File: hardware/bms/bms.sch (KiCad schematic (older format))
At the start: 91 parts

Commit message: Schematics update
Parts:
- added C? (x3): 4.7nF, Capacitor_SMD:C_0603_1608Metric_Pad1.05x0.95mm_HandSolder, symbol Device:C
- added C?: 330uF, Capacitor_Tantalum_SMD:CP_EIA-3528-21_Kemet-B, symbol Device:CP1
- added C?: 1nF, Capacitor_SMD:C_0603_1608Metric_Pad1.05x0.95mm_HandSolder, symbol Device:C
- added C?: 2.2uF, Capacitor_SMD:C_0603_1608Metric_Pad1.05x0.95mm_HandSolder, symbol Device:C
- added D? (x3): MBR340, Diode_THT:D_DO-201AD_P15.24mm_Horizontal, symbol Diode:MBR340
- added JP? (x5): JUMPER, symbol BMS:JUMPER
- added L?: 100uH, symbol pspice:INDUCTOR
- added Q? (x3): Q_NMOS_DGS, symbol Device:Q_NMOS_DGS
- added Q?: Q_PMOS_GSD, symbol BMS:Q_PMOS_GSD
- added Q?: BC817, Package_TO_SOT_SMD:SOT-23, symbol Transistor_BJT:BC817
- added Q?: BS170, Package_TO_SOT_THT:TO-92_Inline, symbol Transistor_FET:BS170
- added R? (x5): 10K, Resistor_SMD:R_0603_1608Metric_Pad1.05x0.95mm_HandSolder, symbol Device:R_Small
- added R? (x6): 1K, Resistor_SMD:R_0603_1608Metric_Pad1.05x0.95mm_HandSolder, symbol Device:R_Small
- added R? (x3): 1M, Resistor_SMD:R_0603_1608Metric_Pad1.05x0.95mm_HandSolder, symbol Device:R_Small
- added R?: 100E, Resistor_SMD:R_0603_1608Metric_Pad1.05x0.95mm_HandSolder, symbol Device:R_Small
- added R? (x2): 499, Resistor_SMD:R_0603_1608Metric_Pad1.05x0.95mm_HandSolder, symbol Device:R_Small
- added R?: 0.002E, Resistor_SMD:R_0603_1608Metric_Pad1.05x0.95mm_HandSolder, symbol Device:R_Small
- added TP? (x2): TestPoint, symbol Connector:TestPoint
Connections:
- net labels added: C1, C1-, C2, C3, C4, C5, C6, C7, C8, CFET, CHG, CHMON, CS1, CS2, DFET, EOC, FETSOFF, INT, LDMON, LOAD, PCFET, PSD, PWM, PWR+, SD, VDD
- net labels removed: CELL1, CELL1-, CELL2, CELL3, CELL4, CELL5, CELL6, CELL7, CELL8, PWM1
- wire segments 329 -> 502
- no-connect marks 4 -> 6
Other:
- note added: "<= 4 Cells"
- note added: "<= 5 Cells"
- note added: "<= 6 Cells"
- note added: "<= 7 Cells"
- note added: "== 3 Cells"
- moved on the sheet: C?

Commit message: added packin and packout
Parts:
- removed J?: Conn_01x10, symbol Connector_Generic:Conn_01x10
- added J? (x4): Conn_01x02, symbol BMS:Conn_01x02
- added J?: Conn_01x10, symbol Connector_Generic:Conn_01x10
- added J?: Conn_01x06, symbol BMS:Conn_01x06
- added J?: Conn_01x04, symbol Connector_Generic:Conn_01x04
- added J?: PACK_OUT, symbol Connector_Generic:Conn_01x04
- added J?: PACK_IN, symbol Connector_Generic:Conn_01x04
- added JP?: JUMPER3, symbol BMS:JUMPER3
- added R?: 2K2, Resistor_SMD:R_0603_1608Metric_Pad1.05x0.95mm_HandSolder, symbol Device:R_Small
- added R?: 300K, Resistor_SMD:R_0603_1608Metric_Pad1.05x0.95mm_HandSolder, symbol Device:R_Small
- added R?: 20K, Resistor_SMD:R_0603_1608Metric_Pad1.05x0.95mm_HandSolder, symbol Device:R_Small
- JP? (x6): symbol BMS:JUMPER -> bms-rescue:JUMPER-BMS
- Q? (x4): symbol BMS:Q_PMOS_GSD -> bms-rescue:Q_PMOS_GSD-BMS
- U?: symbol BMS:LSI94202 -> bms-rescue:LSI94202-BMS
- U?: symbol BMS:TPS560430 -> bms-rescue:TPS560430-BMS
- U?: symbol BMS:USBLC6-2SC6 -> bms-rescue:USBLC6-2SC6-BMS
- Y?: symbol BMS:Crystal -> bms-rescue:Crystal-BMS
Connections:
- net labels added: 485_TX_EN, ADC_PWR, PACK_ID
- net labels removed: ADC, GPIO1, GPIO10, GPIO11, GPIO2, GPIO3, GPIO4, GPIO5
- wire segments 502 -> 558
- no-connect marks 6 -> 8
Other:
- note added: "PACK ID ADC"

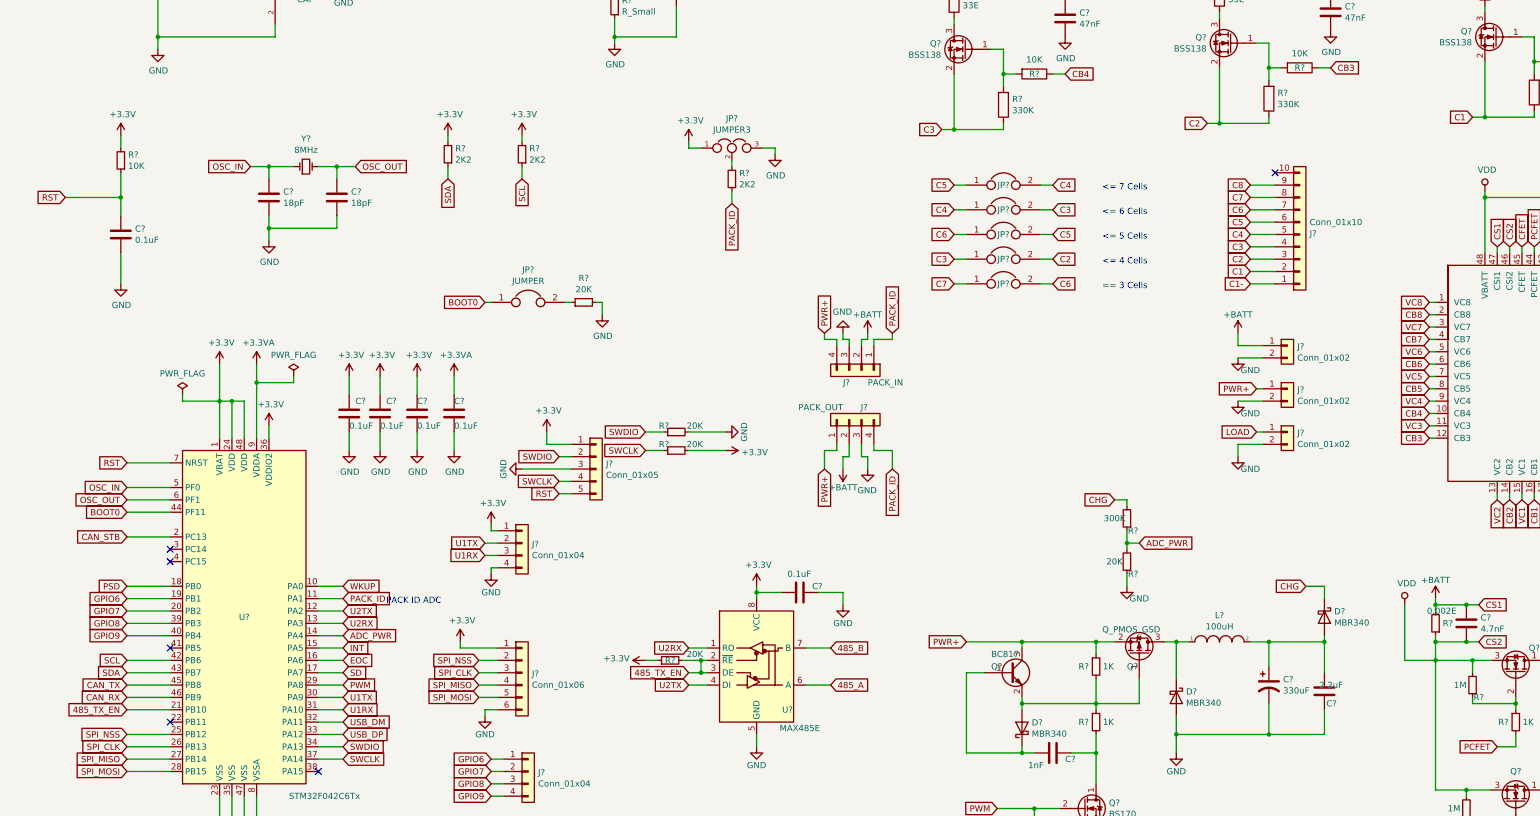
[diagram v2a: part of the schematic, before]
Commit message: Updated power control
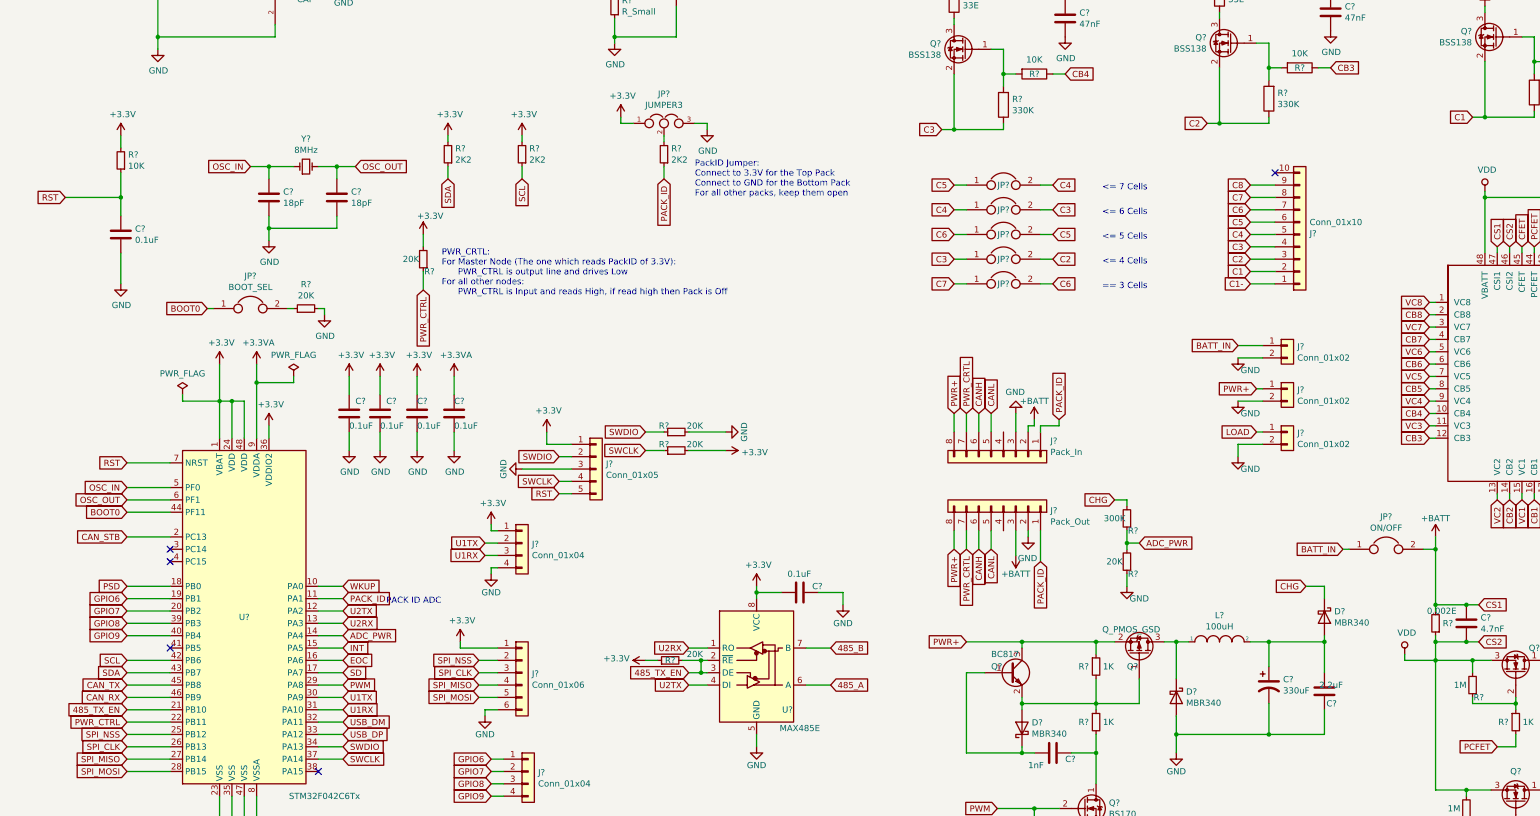
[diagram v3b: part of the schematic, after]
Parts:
- removed J?: PACK_OUT, symbol Connector_Generic:Conn_01x04
- removed J?: PACK_IN, symbol Connector_Generic:Conn_01x04
- added J?: Pack_In, symbol Connector_Generic:Conn_01x08
- added J?: Pack_Out, symbol Connector_Generic:Conn_01x08
- added JP?: ON/OFF, symbol BMS:JUMPER
- added R?: 20K, Resistor_SMD:R_0603_1608Metric_Pad1.05x0.95mm_HandSolder, symbol Device:R_Small
- JP?: value JUMPER -> BOOT_SEL
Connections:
- net +3V3: now also R?.2
- net +BATT: now also J?.2 (Pin_2), J?.3 (Pin_3), JP?.2; no longer J?.1 (Pin_1)
- net CANH: now also J?.6 (Pin_6), J?.6 (Pin_6)
- net CANL: now also J?.5 (Pin_5), J?.5 (Pin_5)
- net GND: now also J?.2 (Pin_2), J?.3 (Pin_3)
- net PACK_ID: now also J?.1 (Pin_1), J?.1 (Pin_1)
- net PWR+: now also J?.8 (Pin_8), J?.8 (Pin_8)
- net PWR_CTRL: now reaches U?.22 (PB11)
- net PWR_CTRL: now also R?.1
- new net BATT_IN: J?.1 (Pin_1), JP?.1
- new net PWR_CRTL: J?.7 (Pin_7), J?.7 (Pin_7)
- no-connect marks 8 -> 7
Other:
- note added: "PWR_CRTL:\nFor Master Node (The one which reads PackID of 3.3V):\n PWR_CTRL is output line and drives Low\nFor all other nodes:\n PWR_CTRL is Input and reads High, if read high then Pack is Off"
- note added: "PackID Jumper:\nConnect to 3.3V for the Top Pack\nConnect to GND for the Bottom Pack\nFor all other packs, keep them open"
- moved on the sheet: JP?, R?

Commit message: added indication leds
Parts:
- removed J?: Conn_01x04, symbol Connector_Generic:Conn_01x04
- added D? (x5): LED, LED_SMD:LED_0805_2012Metric, symbol Device:LED
- added JP? (x2): JUMPER3, symbol BMS:JUMPER3
- added R? (x5): 1K, Resistor_SMD:R_0603_1608Metric_Pad1.05x0.95mm_HandSolder, symbol Device:R_Small
- added TP? (x2): TestPoint, symbol Connector:TestPoint
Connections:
- net PWR_EN is gone; now on an unnamed net: U?.4 (EN)
- net +3V3: now also R?.1, R?.1, R?.1, R?.1, TP?.1
- net 485_A: now also JP?.3
- net 485_B: now also JP?.3
- net CANH: now also JP?.1; no longer J?.6 (Pin_6), J?.6 (Pin_6)
- net CANL: now also JP?.1; no longer J?.5 (Pin_5), J?.5 (Pin_5)
- net CHG: now also R?.1
- net GND: now also D?.1 (K), TP?.1
- net GPIO6 renamed LED_B
- net LED_B: now also D?.1 (K)
- net GPIO7 renamed LED_G
- net LED_G: now also D?.1 (K)
- net GPIO8 renamed LED_Y
- net LED_Y: now also D?.1 (K)
- net GPIO9 renamed LED_R
- net LED_R: now also D?.1 (K)
- new net: D?.2 (A), R?.2 (x5)
- new net Data_H_A: J?.6 (Pin_6), J?.6 (Pin_6), JP?.2
- new net Data_L_B: J?.5 (Pin_5), J?.5 (Pin_5), JP?.2
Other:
- note added: "C1-=GND"
- note added: "C8=+Batt_In"
- moved on the sheet: C?, J?, JP?, Q?, R?, U?
